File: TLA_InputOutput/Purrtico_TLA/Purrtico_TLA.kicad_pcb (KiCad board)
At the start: 2 copper layers, 100 x 50 mm, 60 parts, among them J1 XLR3, J2 Conn_01x03, J3 Conn_01x02, J4 XLR3, J5 Conn_01x02, U1 OPA1679, U2 OPA1679

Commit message: added logo as symbol
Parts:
- added G***: LOGO, LOGO, F.Cu at (132.6, 91.4)

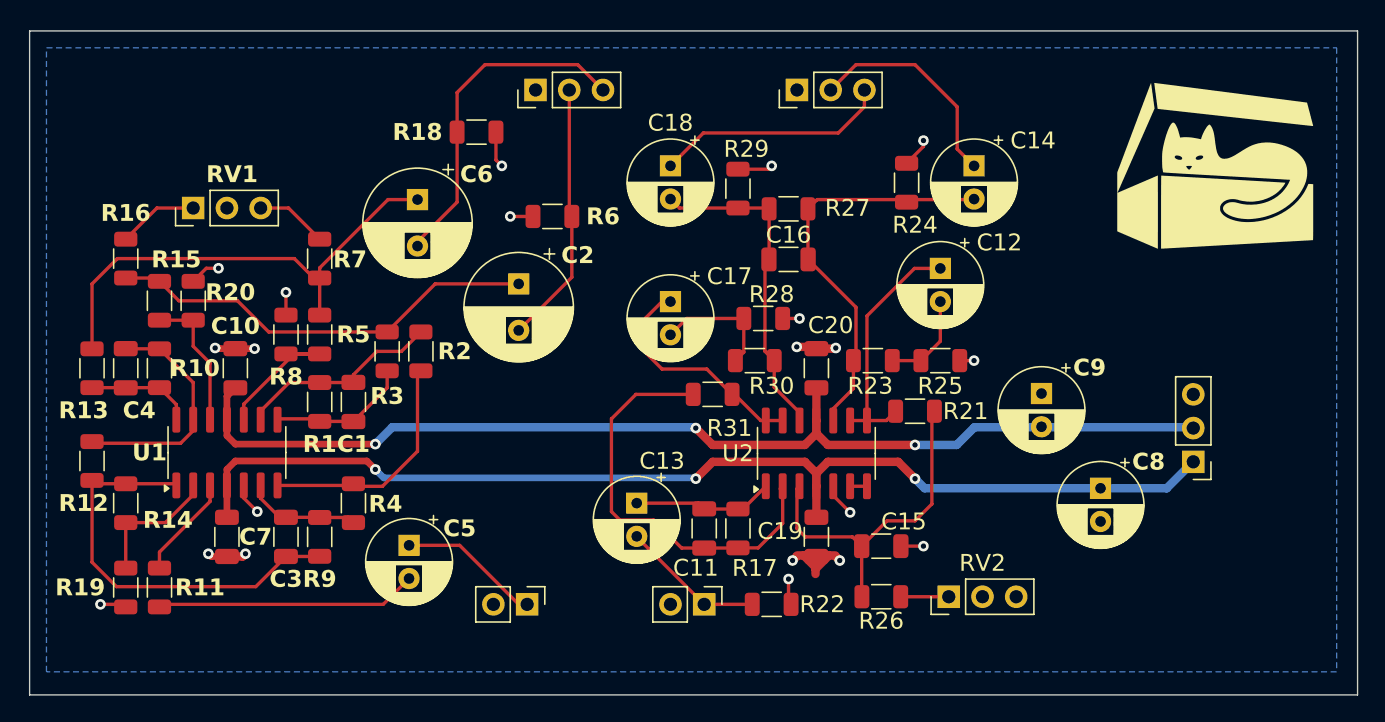
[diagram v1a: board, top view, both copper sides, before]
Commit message: re-oriented resistors
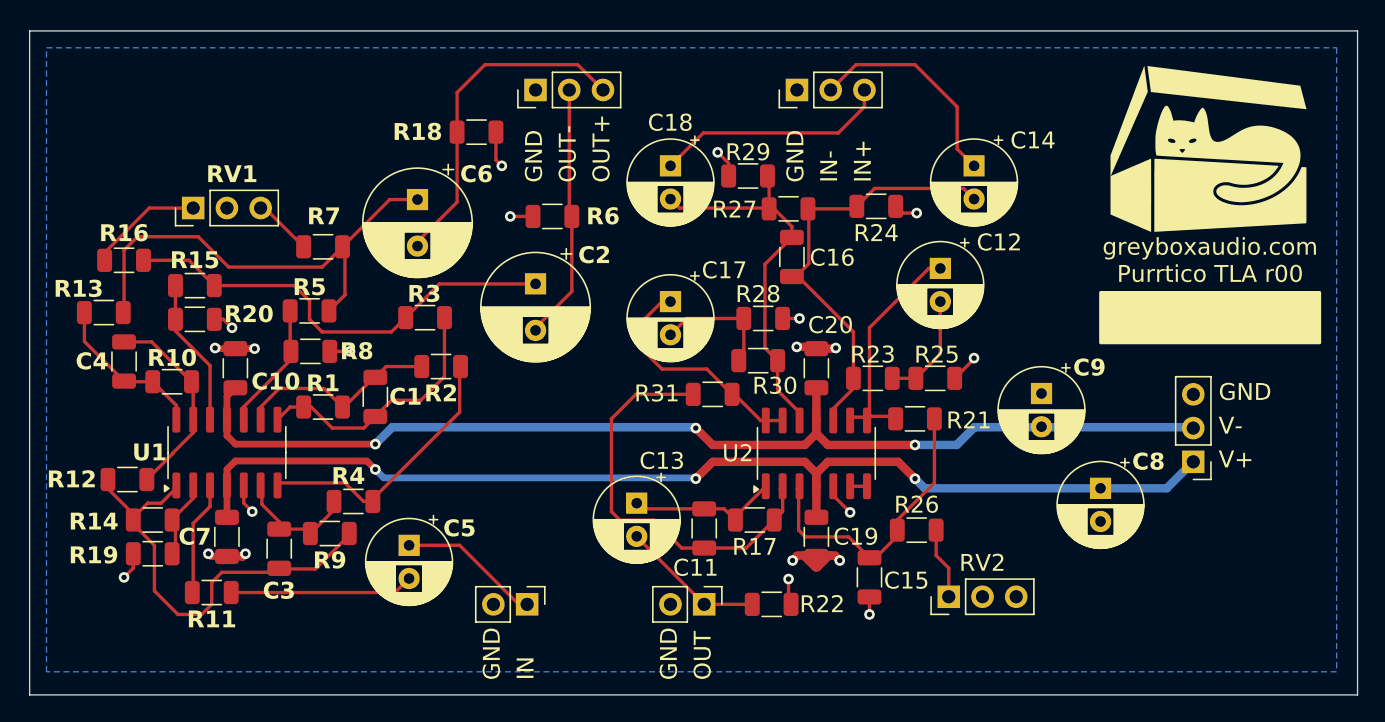
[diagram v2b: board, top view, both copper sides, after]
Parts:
- moved R26 5.68 mm to (110.0, 118.9)
- moved R13 4.28 mm to (48.8, 102.5), turned to 0 degrees
- moved R11 3.96 mm to (56.9, 123.6), turned to 180 degrees
- moved R3 3.82 mm to (73.0, 102.9), turned to 180 degrees
- moved R19 3.25 mm to (52.5, 120.7), turned to 0 degrees
- moved R12 3.01 mm to (50.5, 115.1), turned to 0 degrees
- moved R15 2.90 mm to (55.6, 100.5), turned to 0 degrees
- moved R24 2.90 mm to (106.9, 94.5), turned to 180 degrees
- moved C15 2.51 mm to (106.4, 122.4), turned to -90 degrees
- moved R14 2.40 mm to (52.5, 118.1), turned to 180 degrees
- moved R8 2.24 mm to (64.3, 105.4), turned to 180 degrees
- moved R5 1.93 mm to (64.3, 102.4), turned to 0 degrees
- moved R2 1.91 mm to (74.2, 106.6), turned to 180 degrees
- moved C1 1.69 mm to (69.2, 108.8)
- moved R17 1.42 mm to (97.8, 118.1), turned to 0 degrees
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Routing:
- net Net-(C1-Pad2): track 11.1 -> 20.1 mm
- net Net-(C5-Pad2): track 19.7 -> 13.8 mm
- net Net-(U1A--): track 10.1 -> 5.06 mm
- net Net-(U2D-+): track 24.9 -> 29.1 mm
- net Net-(C4-Pad2): track 8.02 -> 12.2 mm
- net Net-(C3-Pad1): track 32.2 -> 35.3 mm
- net Net-(U1D--): track 17.8 -> 15.2 mm
- net Net-(R2-Pad1): track 18.3 -> 20.9 mm
- net Net-(U2A-+): track 26.2 -> 23.6 mm
- net Net-(R16-Pad2): track 6.05 -> 8.63 mm
- net Net-(U1C-+): track 11.0 -> 8.45 mm
- net Net-(U2C-+): track 31.0 -> 33.0 mm
- net Net-(R26-Pad1): track 3.62 -> 5.41 mm
- net GND: track 41.8 -> 40.1 mm
- net Net-(C2-Pad1): track 33.0 -> 34.4 mm
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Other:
- board text added: "greyboxaudio.com Purrtico TLA r00"

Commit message: update pcb layout
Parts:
- moved R27 3.85 mm to (103.6, 96.6)
- moved R7 2.92 mm to (65.4, 94.6)
- moved R29 2.54 mm to (97.2, 94.7), turned to 0 degrees
- moved J3 2.34 mm to (80.1, 126.7)
- moved J5 2.29 mm to (94.1, 126.7)
- moved R15 2.16 mm to (53.5, 100.6), turned to 180 degrees
- moved R20 2.03 mm to (57.7, 103.0)
- moved R24 1.89 mm to (108.7, 95.1)
- moved R30 1.88 mm to (98.8, 107.8)
- moved R22 1.61 mm to (98.6, 126.0)
- moved C16 1.30 mm to (99.3, 98.6)
- moved C14 1.02 mm to (114.2, 90.4)
- moved C18 0.89 mm to (91.4, 90.6)
- moved R31 0.76 mm to (93.9, 108.7)
- moved R28 0.69 mm to (98.0, 103.5)
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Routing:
- net Net-(J5-Pin_1): track 10.8 -> 13.1 mm
- net Net-(C2-Pad1): track 34.4 -> 36.7 mm
- net Net-(U2C-+): track 33.0 -> 31.6 mm
- net Net-(R7-Pad1): track 4.45 -> 3.36 mm
- net Net-(C6-Pad1): track 35.7 -> 36.7 mm
- net Net-(U2A--): track 31.8 -> 30.8 mm
- net GND: track 40.1 -> 39.4 mm
- net Net-(C11-Pad1): track 12.1 -> 12.6 mm

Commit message: added mounting holes
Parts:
- added H1: MountingHole, MountingHole:MountingHole_3.2mm_M3_DIN965, F.Cu at (47.5, 85.5)
- added H2: MountingHole, MountingHole:MountingHole_3.2mm_M3_DIN965, F.Cu at (138.5, 85.5)
- added H3: MountingHole, MountingHole:MountingHole_3.2mm_M3_DIN965, F.Cu at (47.5, 126.5)
- added H4: MountingHole, MountingHole:MountingHole_3.2mm_M3_DIN965, F.Cu at (138.5, 126.5)
- moved G*** 5.21 mm to (127.0, 89.0)
- moved C14 3.95 mm to (112.0, 87.1)
- moved C12 1.82 mm to (110.0, 99.6)
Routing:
- net Net-(C14-Pad1): track 16.3 -> 12.2 mm
- net Net-(U2C--): track 17.8 -> 16.1 mm
- net Net-(C12-Pad2): track 8.32 -> 7.18 mm
- net Net-(U2C-+): track 31.6 -> 30.8 mm
